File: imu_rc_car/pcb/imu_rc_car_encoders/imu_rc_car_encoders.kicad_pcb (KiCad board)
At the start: 2 copper layers, 66 x 24 mm, 23 parts, among them J1 Conn_01x04_Socket, U1 ITR9608-F, U2 ITR9608-F, U3 LMV393

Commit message: commit #18
added text in encoder board
added pcb layout for car
started car schematic
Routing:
- net GND: vias 93 -> 85
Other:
- board text added: "ENCODER 1"
- board text added: "ENCODER 2"
- board text added: "ENCODER 3"
- board text added: "ENCODER 4"
- board text added: "v1.0.1"
- board text removed: "v1.0"

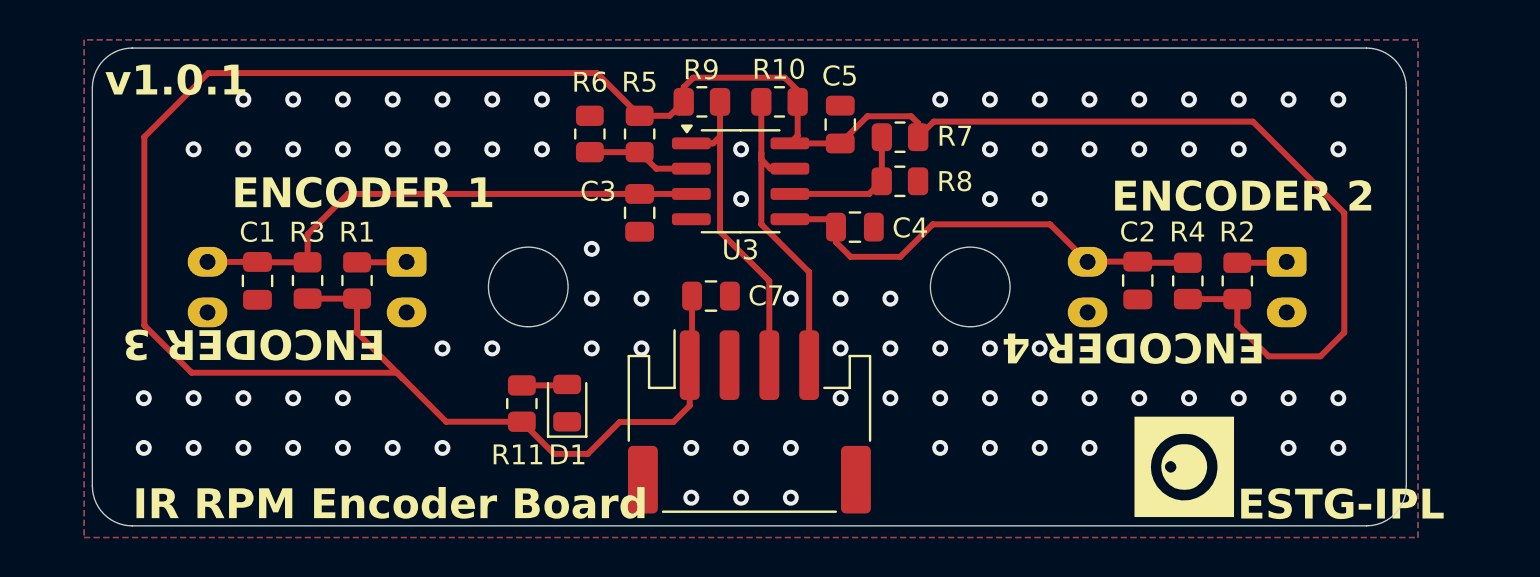
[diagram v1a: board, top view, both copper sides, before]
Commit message: commit #21
changed some dimensions in 3D chassis model
added 3D standoff
added 3D support side motors
backup files are now removed to reduce clutter

IR RPM Encoder Board v1.1.0
changed some dimensions
better layout for JLCPCB
better stitching

src code:
major changes regarding timers and update ticks
refactored all header functions to separate cpp files
refactored pre-compiler lines
better readability
refactored some oled lines
interrupt function buttons have been added
minor changes to led behaviour
data read and send data are now separate processes
bug fix in car stop
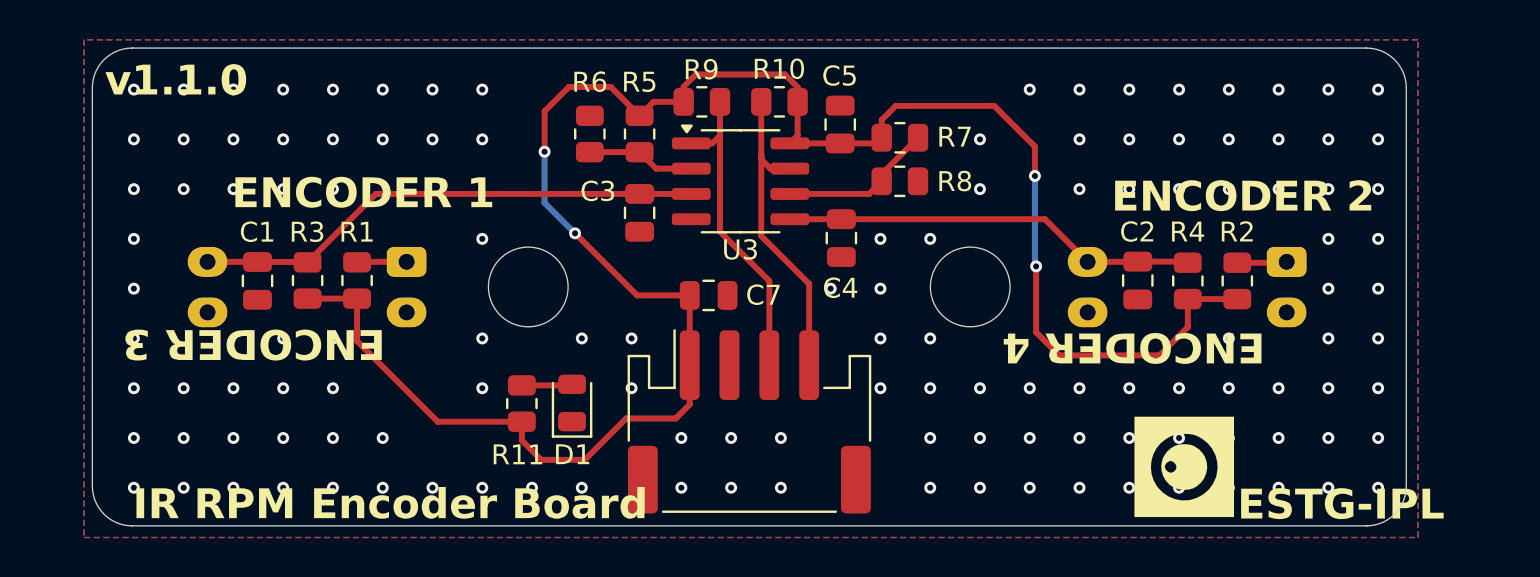
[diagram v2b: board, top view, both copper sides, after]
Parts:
- J1: footprint Connector_JST:JST_PH_S4B-PH-SM4-TB_1x04-1MP_P2.00mm_Horizontal -> IMURCLibrary:JST_PH_S4B-PH-SM4-TB_1x04-1MP_P2.00mm_Horizontal
- moved C4 0.88 mm to (50.0, 22.0), turned to -90 degrees
- moved D1 0.25 mm to (36.5, 30.2)
- moved C7 0.12 mm to (43.4, 24.8)
- turned R7 to 0 degrees
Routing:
- net +3.3V: track 140.7 -> 99.6 mm, vias 0 -> 4
- net Net-(U3B-+): track 22.7 -> 20.9 mm
- net Net-(U3A-+): track 26.6 -> 25.7 mm
- net Net-(U3B--): track 7.10 -> 7.82 mm
- net GND: vias 85 -> 127
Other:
- board text added: "v1.1.0"
- board text added: "{ "ViaStitching": "0.2", "stitch_zone_0": { "HSpacing": "2.5", "VSpacing": "2.5", "HOffset": "0", "VOffset": "0", "Clearance": "0.4", "Randomize": false } }"
- board text removed: "v1.0.1"

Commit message: commit #24
version 2 of proximity sensor case (better results)
updated all M2 holes in pcbs to 2.4mm diameter instead of 2.2mm
updated all M3 holes in pcbs to 3.4mm diameter instead of 3.2mm
minor changes to encoder board
gerber files encoder board
first revision in hand unit
added prox sensor test unit (for test purposes)
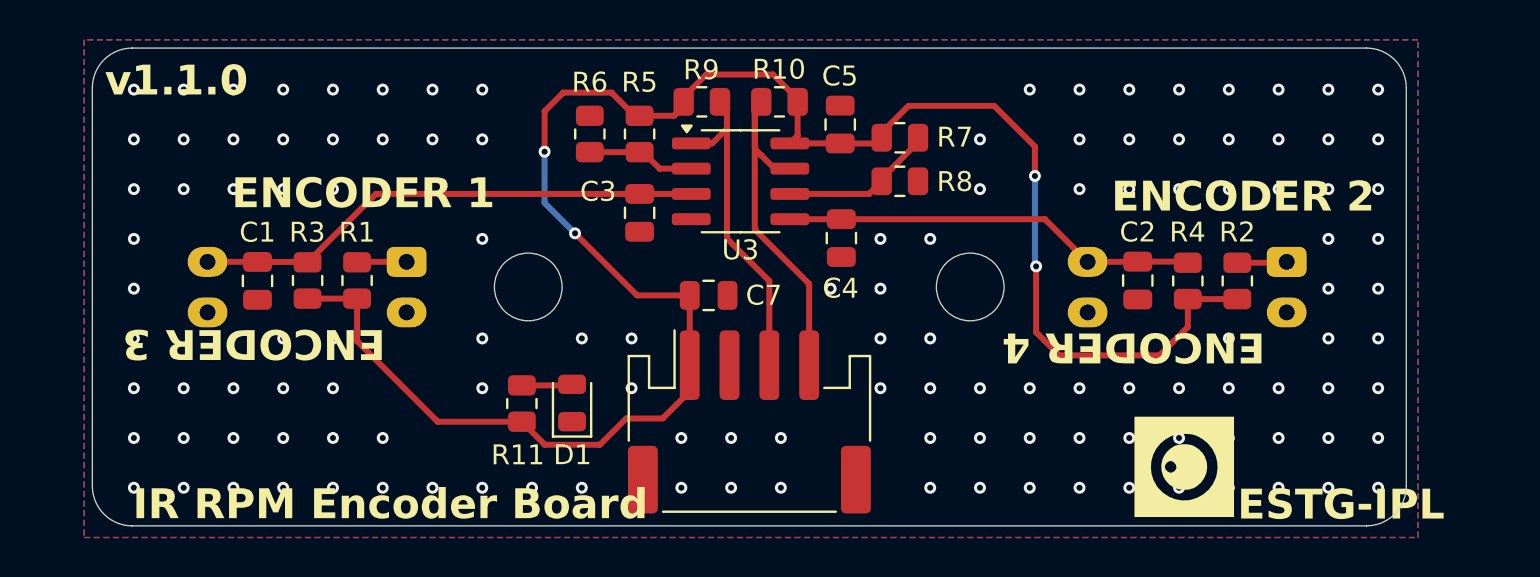
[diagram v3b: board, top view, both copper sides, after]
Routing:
- net +3.3V: track 99.6 -> 96.9 mm
- net ENC2: track 16.1 -> 18.7 mm
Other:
- outline, holes or cut-outs redrawn
- board text removed: "{ "ViaStitching": "0.2", "stitch_zone_0": { "HSpacing": "2.5", "VSpacing": "2.5", "HOffset": "0", "VOffset": "0", "Clearance": "0.4", "Randomize": false } }"

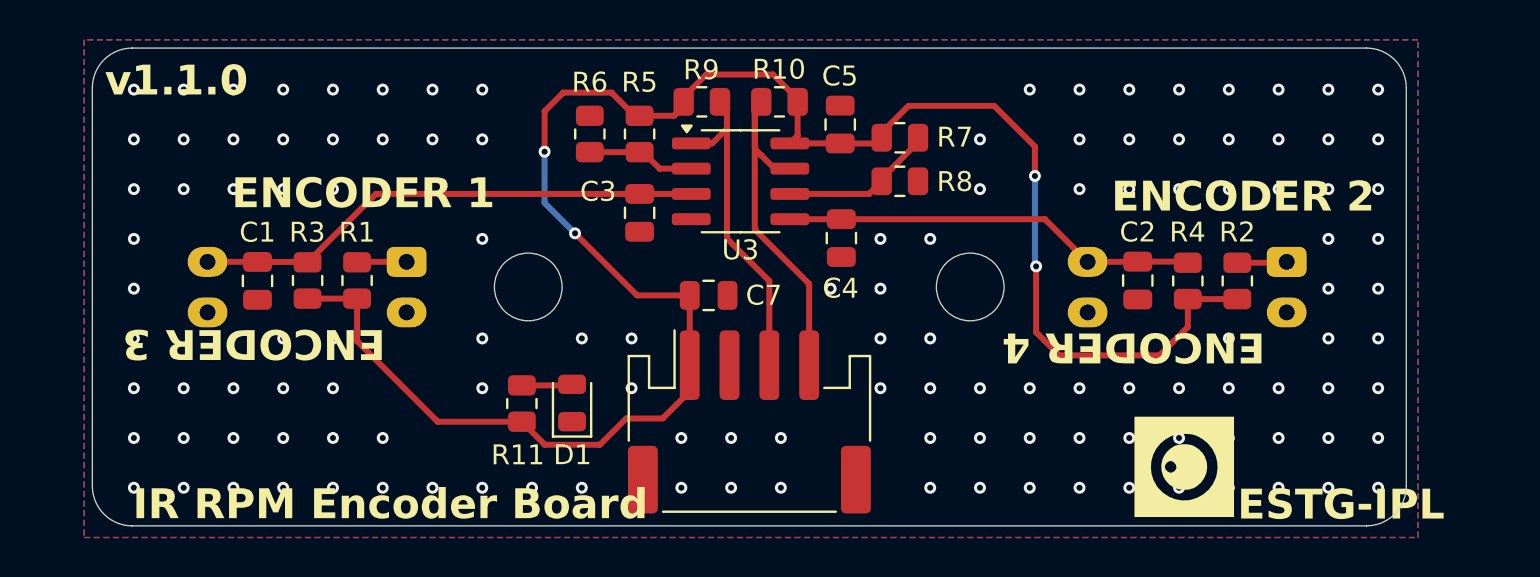
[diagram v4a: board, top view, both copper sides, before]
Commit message: commit #30
changed 3d model offset in esp32s3
imported mouse-bites to kicad
final changes in imu-rc car before revision
critical change in pins 3 and 4 of optical sensor which were switched (encoder board)
removed test unit
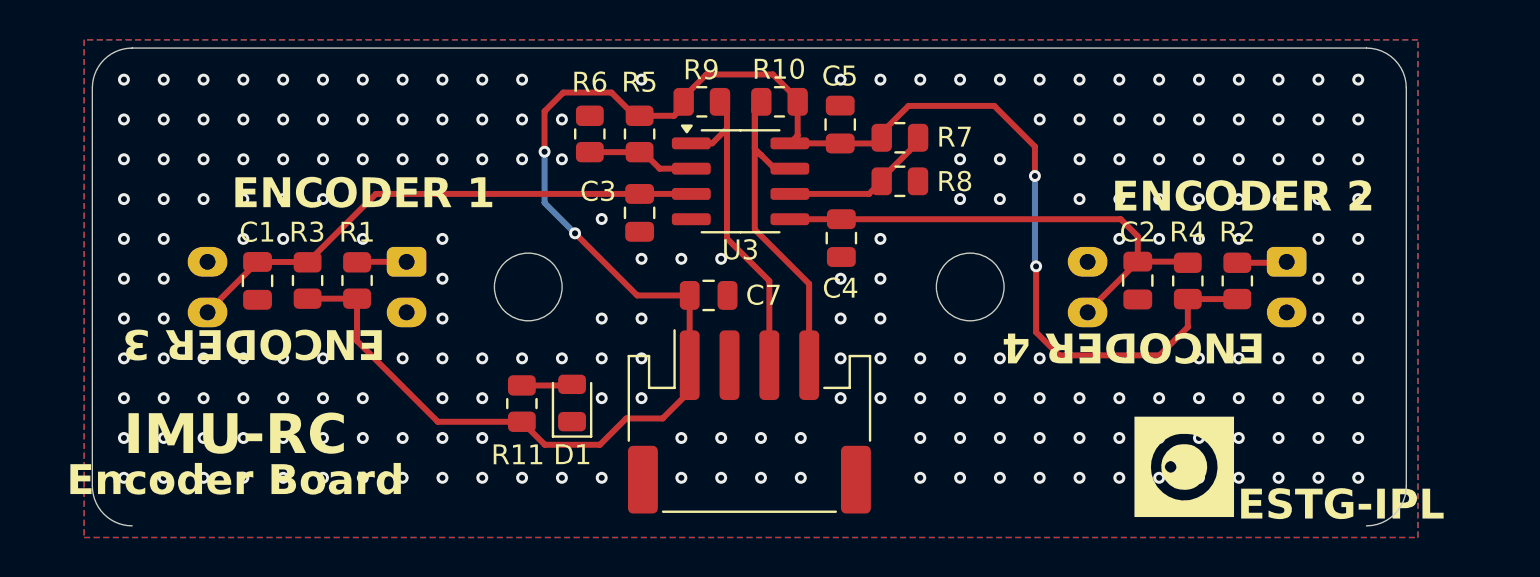
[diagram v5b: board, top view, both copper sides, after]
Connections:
- U1 pad 3: GND -> Net-(U3A-+)
- U1 pad 4: Net-(U3A-+) -> GND
- U2 pad 3: GND -> Net-(U3B-+)
- U2 pad 4: Net-(U3B-+) -> GND
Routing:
- net Net-(U3B-+): track 20.9 -> 25.2 mm
- net Net-(U3A-+): track 25.7 -> 26.8 mm
- net GND: vias 127 -> 222
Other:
- board text added: "Encoder Board"
- board text added: "IMU-RC"
- board text removed: "IR RPM Encoder Board"

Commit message: commit #32
costs table 4
first revision of imu rc car pcb
imu rc encoders final version v1.0.0 (ordered)
imu rc prox sensors final version v1.0.0 (ordered)
minor resistors tolerance changes in hand unit
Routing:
- net GND: vias 222 -> 211
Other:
- board text added: "#chega"
- board text added: "v1.0.0"
- board text removed: "v1.1.0"
